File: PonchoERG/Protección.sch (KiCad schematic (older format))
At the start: 42 parts, among them J1 Entradas Analógicas, U1 TPD4E1B06, U2 TPD4E1B06, U3 TPD4E1B06, U4 TPD4E1B06, U5 TPD4E1B06

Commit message: Actualización 1.0 - Inclusión de nuevos diodos de protección TPD2E001. - Creación de librería TPD2E001 y rediseño de esquemático. - Reubicación de componentes.
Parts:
- removed U1, U2, U3, U4, U5: TPD4E1B06, TO_SOT_Packages_SMD:SOT-23-6, symbol TPD4E1B06
- added U1, U2, U3, U4, U5, U6, U7, U8, U9: TPD2E001, TO_SOT_Packages_SMD:SOT-23-5, symbol TPD2E001
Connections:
- net labels added: +3.3V
- wire segments 141 -> 160
- no-connect marks 7 -> 0
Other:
- moved on the sheet: C1, C10, C11, C12, C13, C14, C15, C16, C2, C3, C4, C5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

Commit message: Reubicación de ADS y componentes pasivos asociados. Sujeto a revisión.
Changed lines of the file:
@@
 LIBS:ADuM2401
 LIBS:ADuM6401
-LIBS:CKCL44X7R1H
-LIBS:GNDD
 LIBS:NetTie
 LIBS:PonchoERG
 LIBS:PonchoERG-cache
-LIBS:Power
-LIBS:VCC
+LIBS:net-tie
+LIBS:TPD2E001
 EELAYER 25 0
 EELAYER END
@@
 	1    0    0    -1
 $EndComp
-Text HLabel 5900 6800 2    60   Output ~ 0
-IN_REF
 Text HLabel 6200 6900 2    60   Input ~ 0
 OUT_DRV_RL
-$Comp
-L GNDD #PWR01
-U 1 1 57C89D0F
-P 1500 7250
-F 0 "#PWR01" H 1500 7000 50  0001 C CNN
-F 1 "GNDD" H 1500 7100 50  0000 C CNN
-F 2 "" H 1500 7250 50  0000 C CNN
-F 3 "" H 1500 7250 50  0000 C CNN
-	1    1500 7250
-	1    0    0    -1
-$EndComp
-$Comp
-L GNDD #PWR02
-U 1 1 57C89D77
-P 5150 7500
-F 0 "#PWR02" H 5150 7250 50  0001 C CNN
-F 1 "GNDD" H 5150 7350 50  0000 C CNN
-F 2 "" H 5150 7500 50  0000 C CNN
-F 3 "" H 5150 7500 50  0000 C CNN
-	1    5150 7500
-	1    0    0    -1
-$EndComp
-$Comp
-L GNDD #PWR03
-U 1 1 57C89DDF
-P 6450 6400
-F 0 "#PWR03" H 6450 6150 50  0001 C CNN
-F 1 "GNDD" H 6450 6250 50  0000 C CNN
-F 2 "" H 6450 6400 50  0000 C CNN
-F 3 "" H 6450 6400 50  0000 C CNN
-	1    6450 6400
-	1    0    0    -1
-$EndComp
-$Comp
-L GNDD #PWR04
-U 1 1 57C89E47
-P 6450 4900
-F 0 "#PWR04" H 6450 4650 50  0001 C CNN
-F 1 "GNDD" H 6450 4750 50  0000 C CNN
-F 2 "" H 6450 4900 50  0000 C CNN
-F 3 "" H 6450 4900 50  0000 C CNN
-	1    6450 4900
-	1    0    0    -1
-$EndComp
-$Comp
-L GNDD #PWR05
-U 1 1 57C89EAF
-P 6450 3400
-F 0 "#PWR05" H 6450 3150 50  0001 C CNN
-F 1 "GNDD" H 6450 3250 50  0000 C CNN
-F 2 "" H 6450 3400 50  0000 C CNN
-F 3 "" H 6450 3400 50  0000 C CNN
-	1    6450 3400
-	1    0    0    -1
-$EndComp
-$Comp
-L GNDD #PWR06
-U 1 1 57C89F17
-P 6400 1900
-F 0 "#PWR06" H 6400 1650 50  0001 C CNN
-F 1 "GNDD" H 6400 1750 50  0000 C CNN
-F 2 "" H 6400 1900 50  0000 C CNN
-F 3 "" H 6400 1900 50  0000 C CNN
-	1    6400 1900
-	1    0    0    -1
-$EndComp
 $Comp
 L TPD2E001 U1
@@
 	0    -1   -1   0
 $EndComp
-$Comp
-L +3.3V #PWR07
-U 1 1 57C67D85
-P 1200 7250
-F 0 "#PWR07" H 1200 7100 50  0001 C CNN
-F 1 "+3.3V" H 1200 7390 50  0000 C CNN
-F 2 "" H 1200 7250 50  0000 C CNN
-F 3 "" H 1200 7250 50  0000 C CNN
-	1    1200 7250
-	-1   0    0    1
-$EndComp
 Wire Wire Line
 	2650 2200 2650 1100
@@
 	2150 6800 3750 6800
 Wire Wire Line
-	3950 6800 5900 6800
-Wire Wire Line
 	2050 6900 3950 6900
 Wire Wire Line
@@
 	4200 1200 4200 1000
 Connection ~ 4200 1000
-Wire Wire Line
-	3100 2000 3100 2050
 Wire Wire Line
 	2800 2050 3950 2050
@@
 Connection ~ 2800 5050
 Connection ~ 3050 5050
+Wire Wire Line
+	3100 2050 3100 2000
+Wire Wire Line
+	3950 6800 5900 6800
+Text HLabel 5900 6800 2    60   Output ~ 0
+IN_REF
+Text GLabel 6400 1900 3    60   Output ~ 0
+GNDD
+Text GLabel 1500 7250 3    60   Output ~ 0
+GNDD
+Text GLabel 6450 3400 3    60   Output ~ 0
+GNDD
+Text GLabel 6450 4900 3    60   Output ~ 0
+GNDD
+Text GLabel 6450 6400 3    60   Output ~ 0
+GNDD
+Text GLabel 5150 7500 3    60   Output ~ 0
+GNDD
+Text GLabel 1200 7250 3    60   Input ~ 0
++3.3V
 $EndSCHEMATC

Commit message: Subida n.0
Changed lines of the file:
@@
 Connection ~ 1450 5900
 Wire Wire Line
-	1500 7250 1500 6850
-Wire Wire Line
-	6400 1900 6400 1850
+	1500 6850 1500 7250
+Wire Wire Line
+	6400 1850 6400 1900
 Wire Wire Line
 	6100 1450 6100 1850
@@
 	6700 1850 6700 1750
 Wire Wire Line
-	6450 3400 6450 3350
+	6450 3350 6450 3400
 Wire Wire Line
 	6150 2950 6150 3350
@@
 	6750 3350 6750 3250
 Wire Wire Line
-	6450 4900 6450 4850
+	6450 4850 6450 4900
 Wire Wire Line
 	6150 4450 6150 4850
@@
 	6750 4850 6750 4750
 Wire Wire Line
-	6450 6400 6450 6350
+	6450 6350 6450 6400
 Wire Wire Line
 	6150 5950 6150 6350
@@
 	1150 700  5000 700
 Wire Wire Line
-	5200 800  1150 800
+	1150 800  5200 800
 Wire Wire Line
 	1150 900  5400 900
 Wire Wire Line
-	5600 1000 1150 1000
+	1150 1000 5600 1000
 Wire Wire Line
 	3150 1200 3150 700
@@
 	2050 3900 5450 3900
 Wire Wire Line
-	5650 4000 1950 4000
+	1950 4000 5650 4000
 Wire Wire Line
 	3100 2700 3100 2200
@@
 Connection ~ 3350 3600
 Wire Wire Line
-	1200 7250 1200 6850
+	1200 6850 1200 7250
 Wire Wire Line
 	2800 2050 2800 7000

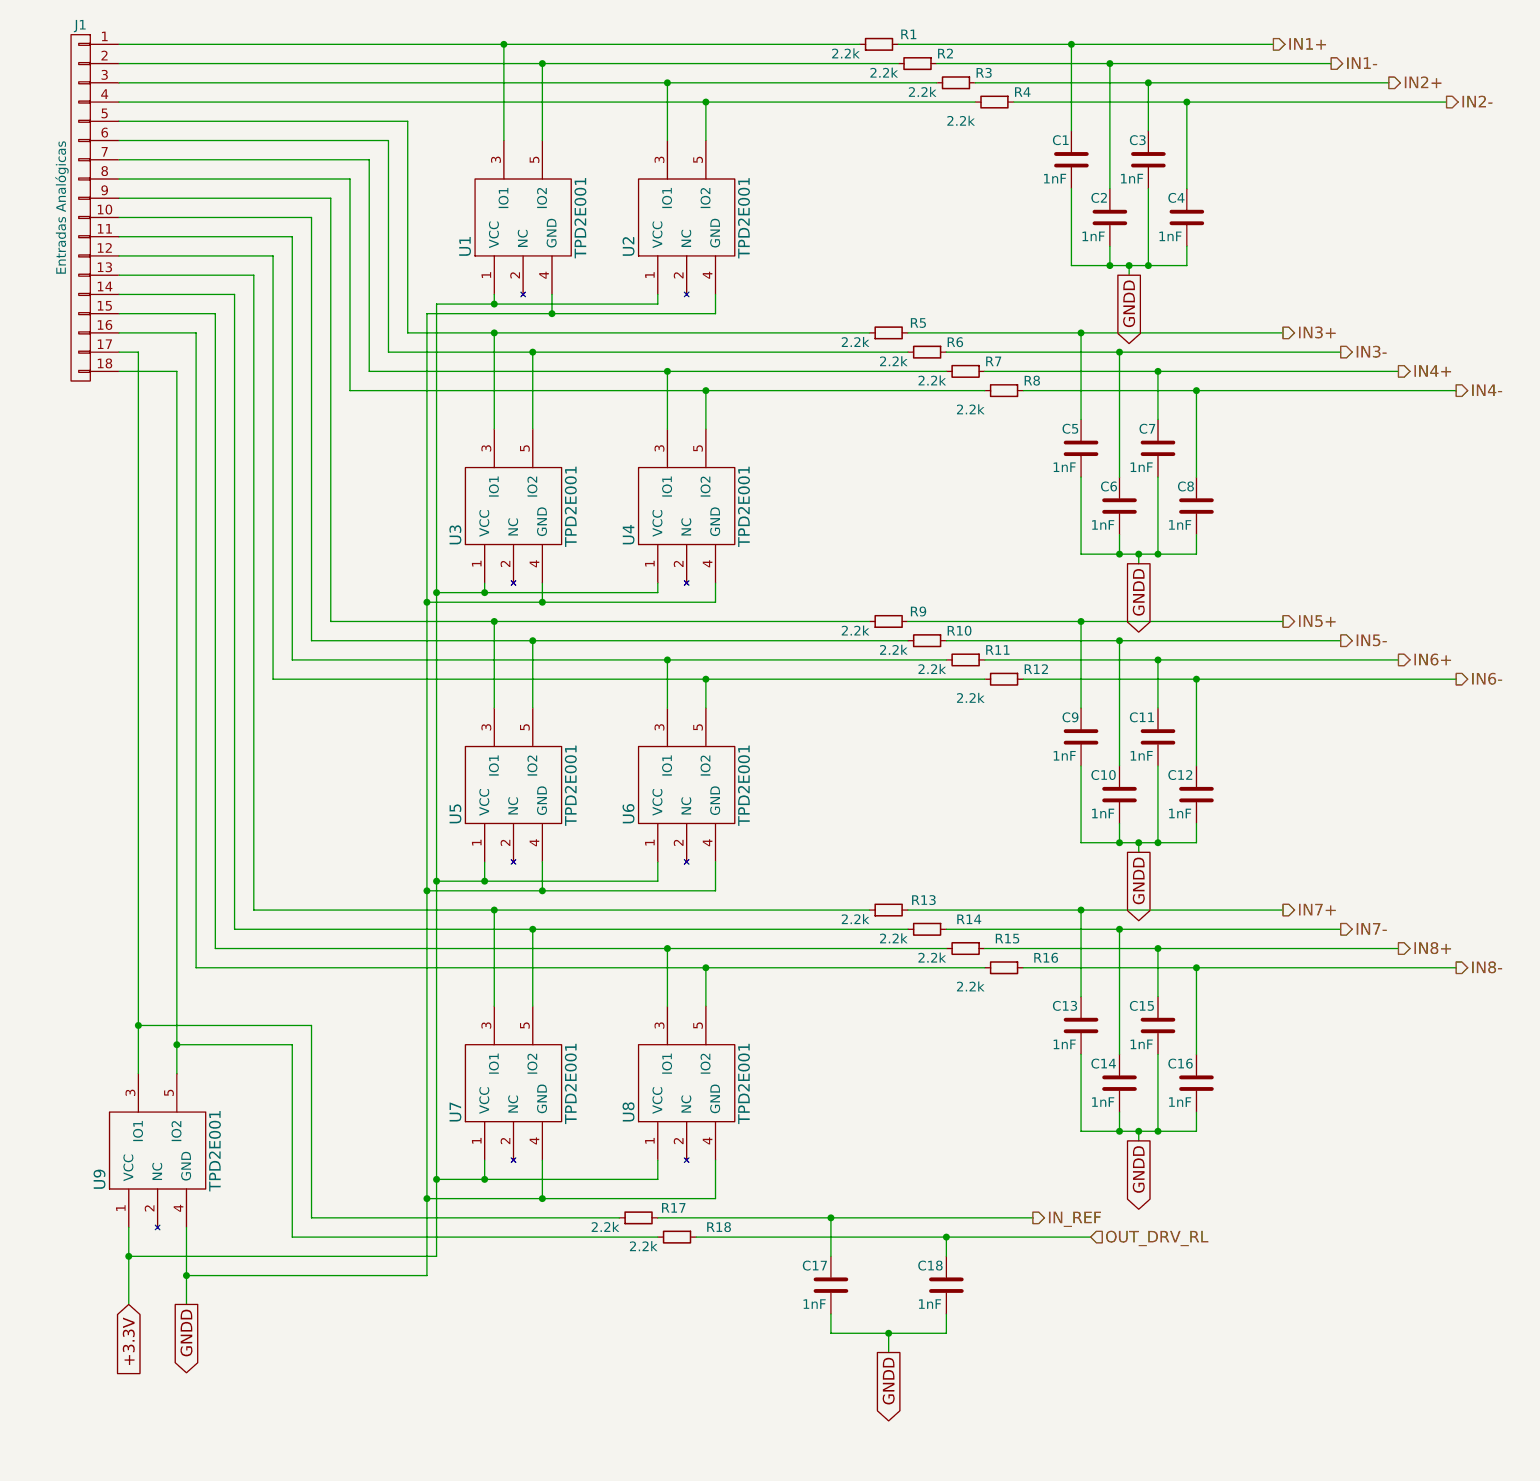
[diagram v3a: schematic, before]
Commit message: Última actualización del proyecto. Creación de librería única "PonchoERG.lib" con todos los componentes. Se agregó el conector estilo CIAA para conectar SPI y alimentaciones. Se agregó carpeta con archivos para creación de lista de materiales "PonchoERG.xml" provisoria. Se modificaron todos los pines de alimentación que estaban como etiquetas con los correspondientes. Quedaría solucionar los problemas del ERC respecto a los errores de pines con el famoso PWR_FLAG.
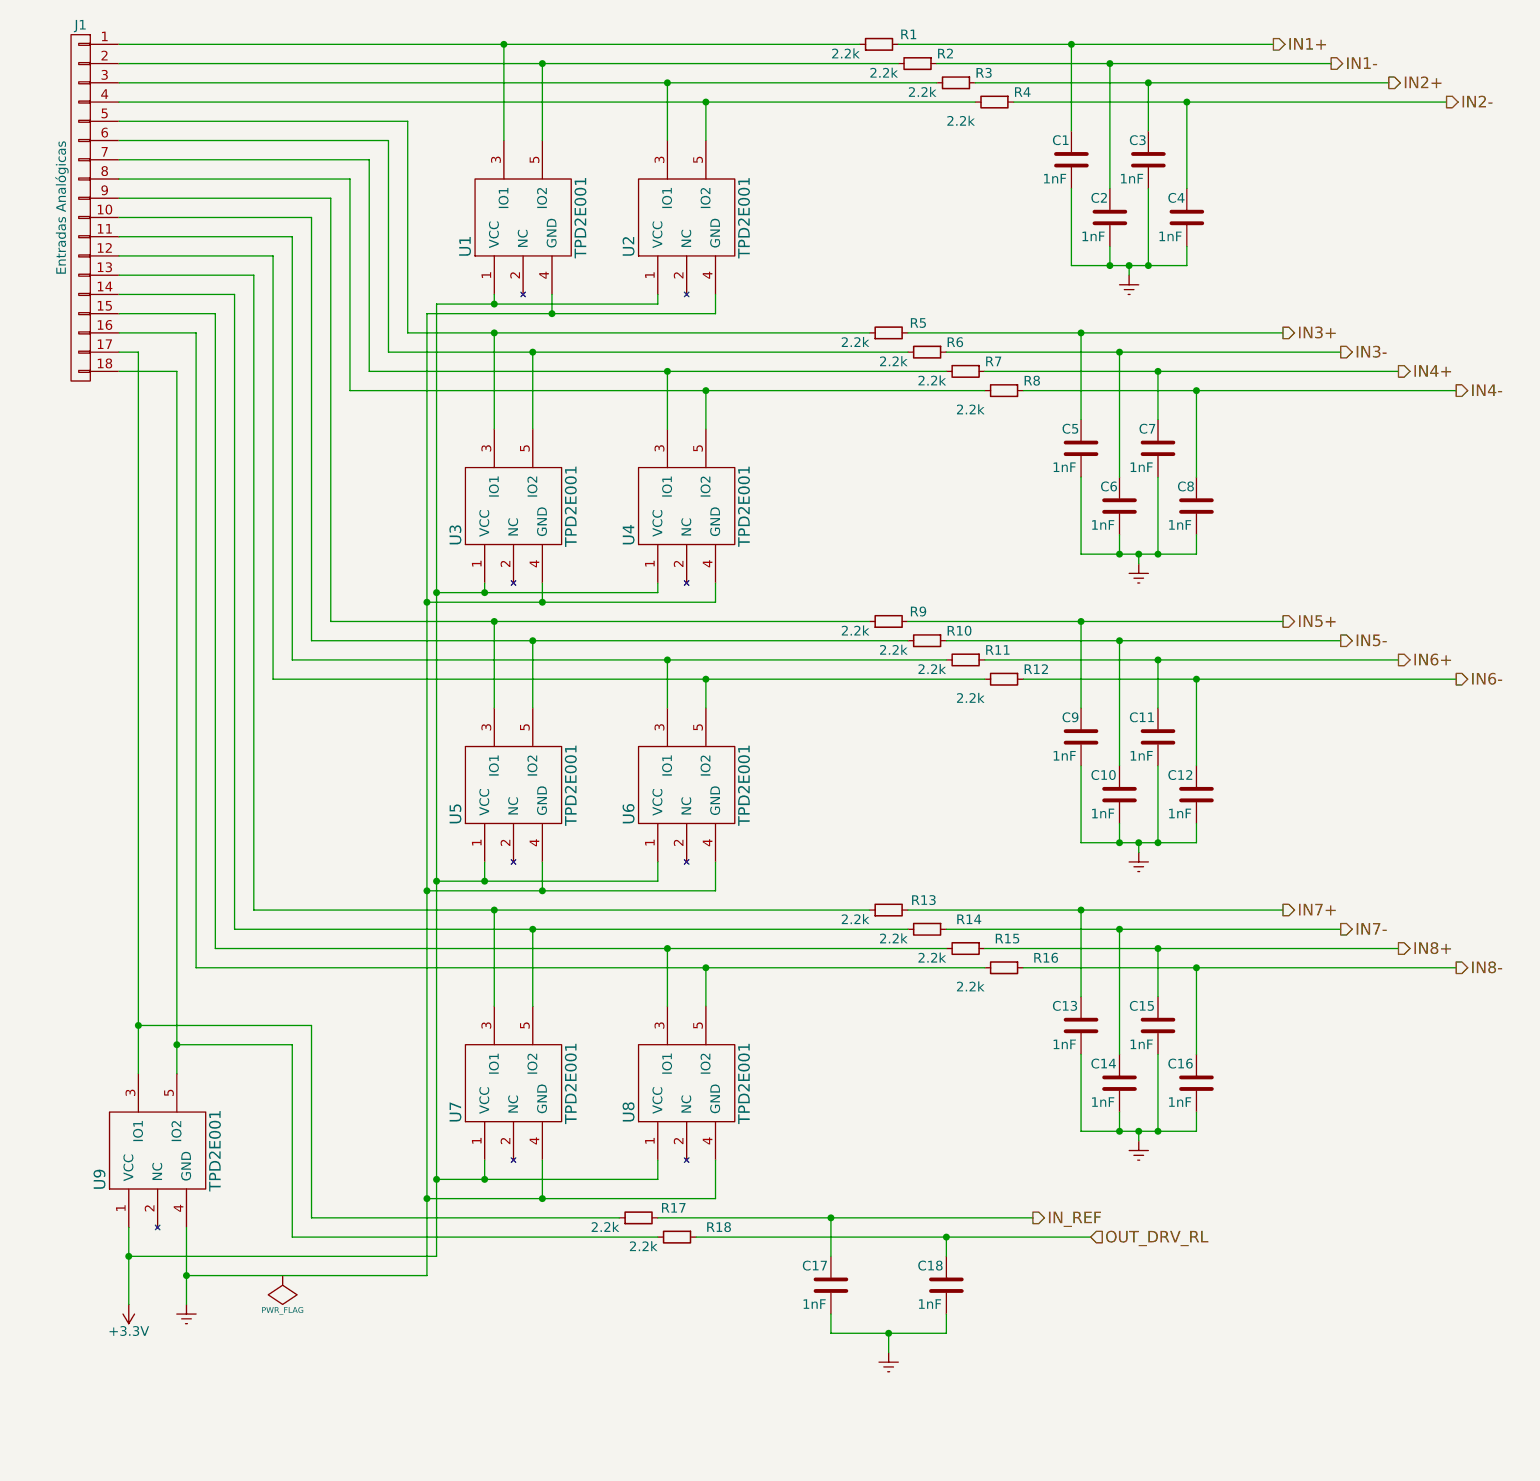
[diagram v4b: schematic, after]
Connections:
- net +3.3V renamed +3V3
- net GNDD renamed Earth
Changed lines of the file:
@@
 EESchema Schematic File Version 2
 LIBS:PonchoERG-rescue
-LIBS:74xgxx
-LIBS:74xx
-LIBS:ac-dc
-LIBS:actel
-LIBS:adc-dac
-LIBS:Altera
-LIBS:analog_devices
-LIBS:analog_switches
-LIBS:atmel
-LIBS:audio
-LIBS:brooktre
-LIBS:cmos_ieee
-LIBS:cmos4000
-LIBS:conn
-LIBS:contrib
-LIBS:cypress
-LIBS:dc-dc
-LIBS:device
-LIBS:digital-audio
-LIBS:diode
-LIBS:display
-LIBS:dsp
-LIBS:elec-unifil
-LIBS:ESD_Protection
-LIBS:ftdi
-LIBS:gennum
-LIBS:graphic
-LIBS:hc11
-LIBS:intel
-LIBS:interface
-LIBS:ir
-LIBS:Lattice
-LIBS:linear
-LIBS:logo
-LIBS:maxim
-LIBS:memory
-LIBS:microchip
-LIBS:microchip_dspic33dsc
-LIBS:microchip_pic10mcu
-LIBS:microchip_pic12mcu
-LIBS:microchip_pic16mcu
-LIBS:microchip_pic18mcu
-LIBS:microchip_pic32mcu
-LIBS:microcontrollers
-LIBS:motor_drivers
-LIBS:motorola
-LIBS:msp430
-LIBS:nordicsemi
-LIBS:nxp_armmcu
-LIBS:onsemi
-LIBS:opto
-LIBS:Oscillators
-LIBS:philips
+LIBS:Misc_Poncho_Grande
+LIBS:Poncho_Esqueleto
+LIBS:PonchoERG
 LIBS:power
-LIBS:Power_Management
-LIBS:powerint
-LIBS:pspice
-LIBS:references
-LIBS:regul
-LIBS:relays
-LIBS:rfcom
-LIBS:sensors
-LIBS:silabs
-LIBS:siliconi
-LIBS:stm8
-LIBS:stm32
-LIBS:supertex
-LIBS:switches
-LIBS:texas
-LIBS:transf
-LIBS:transistors
-LIBS:ttl_ieee
-LIBS:valves
-LIBS:video
-LIBS:Xicor
-LIBS:xilinx
-LIBS:Zilog
-LIBS:ADS1299
-LIBS:ADuM2401
-LIBS:ADuM6401
-LIBS:NetTie
-LIBS:PonchoERG
 LIBS:PonchoERG-cache
-LIBS:net-tie
-LIBS:TPD2E001
 EELAYER 25 0
 EELAYER END
@@
 Text HLabel 5900 6800 2    60   Output ~ 0
 IN_REF
-Text GLabel 6400 1900 3    60   Output ~ 0
-GNDD
-Text GLabel 1500 7250 3    60   Output ~ 0
-GNDD
-Text GLabel 6450 3400 3    60   Output ~ 0
-GNDD
-Text GLabel 6450 4900 3    60   Output ~ 0
-GNDD
-Text GLabel 6450 6400 3    60   Output ~ 0
-GNDD
-Text GLabel 5150 7500 3    60   Output ~ 0
-GNDD
-Text GLabel 1200 7250 3    60   Input ~ 0
-+3.3V
+$Comp
+L +3.3V-RESCUE-PonchoERG #PWR?
+U 1 1 57CB28B5
+P 1200 7250
+AR Path="/57CB28B5" Ref="#PWR?"  Part="1"
+AR Path="/57BDBDC8/57CB28B5" Ref="#PWR01"  Part="1"
+F 0 "#PWR01" H 1200 7100 50  0001 C CNN
+F 1 "+3.3V" H 1200 7390 50  0000 C CNN
+F 2 "" H 1200 7250 50  0000 C CNN
+F 3 "" H 1200 7250 50  0000 C CNN
+	1    1200 7250
+	-1   0    0    1
+$EndComp
+$Comp
+L Earth #PWR02
+U 1 1 57CB2925
+P 1500 7250
+F 0 "#PWR02" H 1500 7000 50  0001 C CNN
+F 1 "Earth" H 1500 7100 50  0001 C CNN
+F 2 "" H 1500 7250 50  0000 C CNN
+F 3 "" H 1500 7250 50  0000 C CNN
+	1    1500 7250
+	1    0    0    -1
+$EndComp
+$Comp
+L Earth #PWR03
+U 1 1 57CB2C47
+P 5150 7500
+F 0 "#PWR03" H 5150 7250 50  0001 C CNN
+F 1 "Earth" H 5150 7350 50  0001 C CNN
+F 2 "" H 5150 7500 50  0000 C CNN
+F 3 "" H 5150 7500 50  0000 C CNN
+	1    5150 7500
+	1    0    0    -1
+$EndComp
+$Comp
+L Earth #PWR04
+U 1 1 57CB2CB7
+P 6450 6400
+F 0 "#PWR04" H 6450 6150 50  0001 C CNN
+F 1 "Earth" H 6450 6250 50  0001 C CNN
+F 2 "" H 6450 6400 50  0000 C CNN
+F 3 "" H 6450 6400 50  0000 C CNN
+	1    6450 6400
+	1    0    0    -1
+$EndComp
+$Comp
+L Earth #PWR05
+U 1 1 57CB2D27
+P 6450 4900
+F 0 "#PWR05" H 6450 4650 50  0001 C CNN
+F 1 "Earth" H 6450 4750 50  0001 C CNN
+F 2 "" H 6450 4900 50  0000 C CNN
+F 3 "" H 6450 4900 50  0000 C CNN
+	1    6450 4900
+	1    0    0    -1
+$EndComp
+$Comp
+L Earth #PWR06
+U 1 1 57CB3077
+P 6400 1900
+F 0 "#PWR06" H 6400 1650 50  0001 C CNN
+F 1 "Earth" H 6400 1750 50  0001 C CNN
+F 2 "" H 6400 1900 50  0000 C CNN
+F 3 "" H 6400 1900 50  0000 C CNN
+	1    6400 1900
+	1    0    0    -1
+$EndComp
+$Comp
+L Earth #PWR07
+U 1 1 57CB30E7
+P 6450 3400
+F 0 "#PWR07" H 6450 3150 50  0001 C CNN
+F 1 "Earth" H 6450 3250 50  0001 C CNN
+F 2 "" H 6450 3400 50  0000 C CNN
+F 3 "" H 6450 3400 50  0000 C CNN
+	1    6450 3400
+	1    0    0    -1
+$EndComp
+$Comp
+L PWR_FLAG #FLG014
+U 1 1 57CB771E
+P 2000 7100
+F 0 "#FLG014" H 2000 7195 30  0001 C CNN
+F 1 "PWR_FLAG" H 2000 7280 30  0000 C CNN
+F 2 "" H 2000 7100 60  0000 C CNN
+F 3 "" H 2000 7100 60  0000 C CNN
+	1    2000 7100
+	-1   0    0    1
+$EndComp
 $EndSCHEMATC

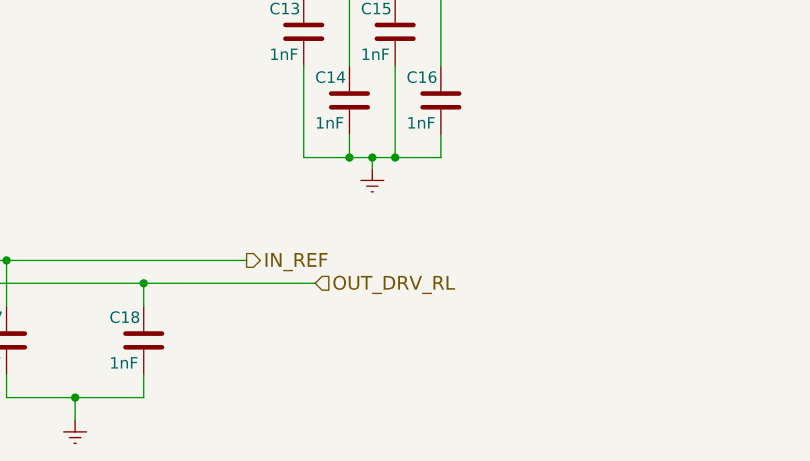
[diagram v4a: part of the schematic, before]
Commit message: Inclusión en esquemáticos de los nuevos bloques de circuitos para la utilización de las líneas del BIAS. Actualización de librería de proyecto. Objetivo de este comit: revisar actualización e inclusión de BIAS.
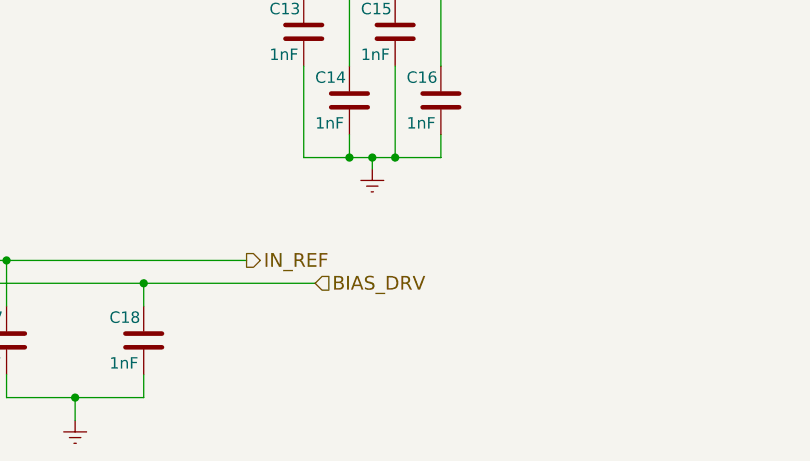
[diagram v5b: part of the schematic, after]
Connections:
- net OUT_DRV_RL renamed BIAS_DRV
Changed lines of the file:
@@
 LIBS:PonchoERG
 LIBS:power
+LIBS:74xgxx
+LIBS:74xx
+LIBS:ac-dc
+LIBS:actel
+LIBS:adc-dac
+LIBS:Altera
+LIBS:analog_devices
+LIBS:analog_switches
+LIBS:atmel
+LIBS:audio
+LIBS:brooktre
+LIBS:cmos_ieee
+LIBS:cmos4000
+LIBS:conn
+LIBS:contrib
+LIBS:cypress
+LIBS:dc-dc
+LIBS:device
+LIBS:digital-audio
+LIBS:diode
+LIBS:display
+LIBS:dsp
+LIBS:elec-unifil
+LIBS:ESD_Protection
+LIBS:ftdi
+LIBS:gennum
+LIBS:graphic
+LIBS:hc11
+LIBS:intel
+LIBS:interface
+LIBS:ir
+LIBS:Lattice
+LIBS:linear
+LIBS:logo
+LIBS:maxim
+LIBS:memory
+LIBS:microchip
+LIBS:microchip_dspic33dsc
+LIBS:microchip_pic10mcu
+LIBS:microchip_pic12mcu
+LIBS:microchip_pic16mcu
+LIBS:microchip_pic18mcu
+LIBS:microchip_pic32mcu
+LIBS:microcontrollers
+LIBS:motor_drivers
+LIBS:motorola
+LIBS:msp430
+LIBS:nordicsemi
+LIBS:nxp_armmcu
+LIBS:onsemi
+LIBS:opto
+LIBS:Oscillators
+LIBS:philips
+LIBS:Power_Management
+LIBS:powerint
+LIBS:pspice
+LIBS:references
+LIBS:regul
+LIBS:relays
+LIBS:rfcom
+LIBS:sensors
+LIBS:silabs
+LIBS:siliconi
+LIBS:stm8
+LIBS:stm32
+LIBS:supertex
+LIBS:switches
+LIBS:texas
+LIBS:transf
+LIBS:transistors
+LIBS:ttl_ieee
+LIBS:valves
+LIBS:video
+LIBS:Xicor
+LIBS:xilinx
+LIBS:Zilog
 LIBS:PonchoERG-cache
 EELAYER 25 0
@@
 $EndComp
 Text HLabel 6200 6900 2    60   Input ~ 0
-OUT_DRV_RL
+BIAS_DRV
 $Comp
 L TPD2E001 U1
